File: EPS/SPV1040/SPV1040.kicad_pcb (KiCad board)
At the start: 2 copper layers, 17 parts, among them U1 SPV1040

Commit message: adding TSSOP8 footprint into SS footprint library for SPV1040. Also referenced footprint to the one in SS within the PCB layout
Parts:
- U1: footprint digikey-footprints:TSSOP-8_W4.4mm -> SS:TSSOP-8_W4.4mm

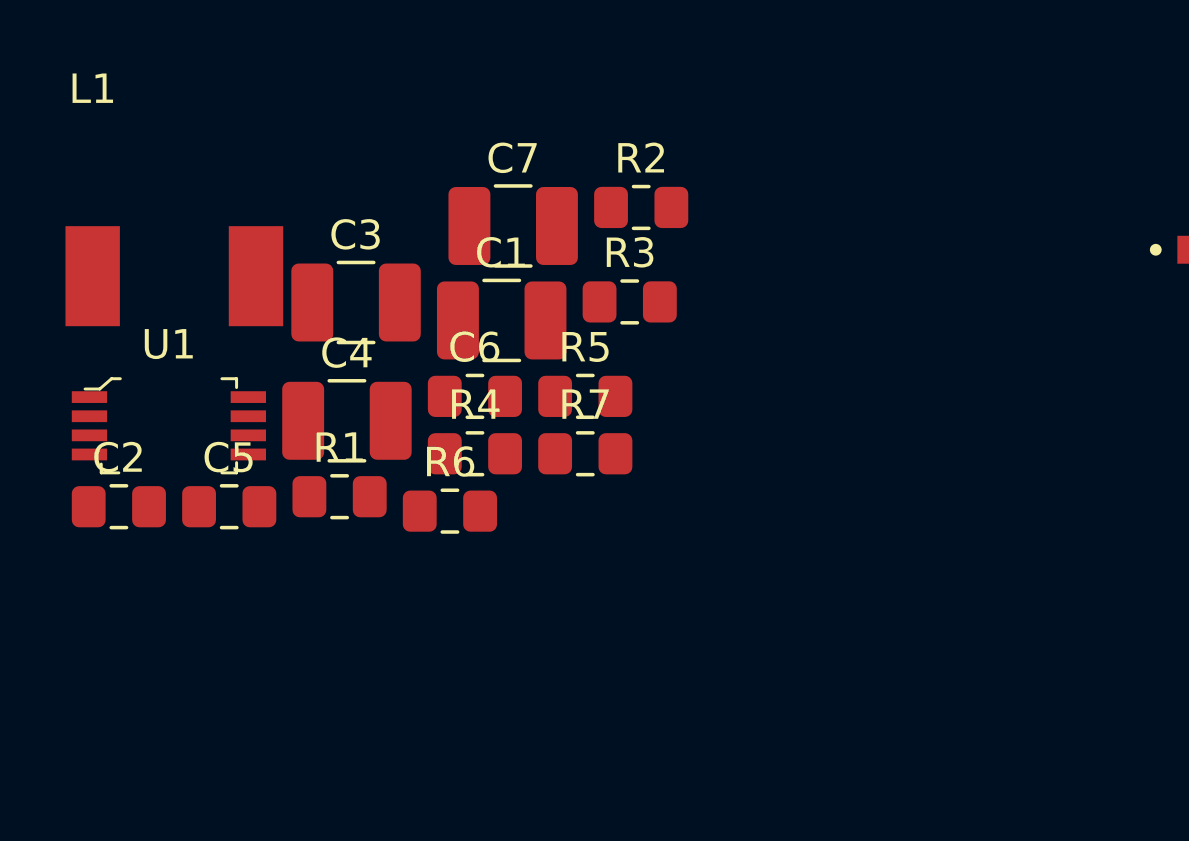
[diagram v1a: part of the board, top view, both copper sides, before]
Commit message: creating python script to find trace width for certian resistance. Also updating resistor divider feedback python to take user input to quit
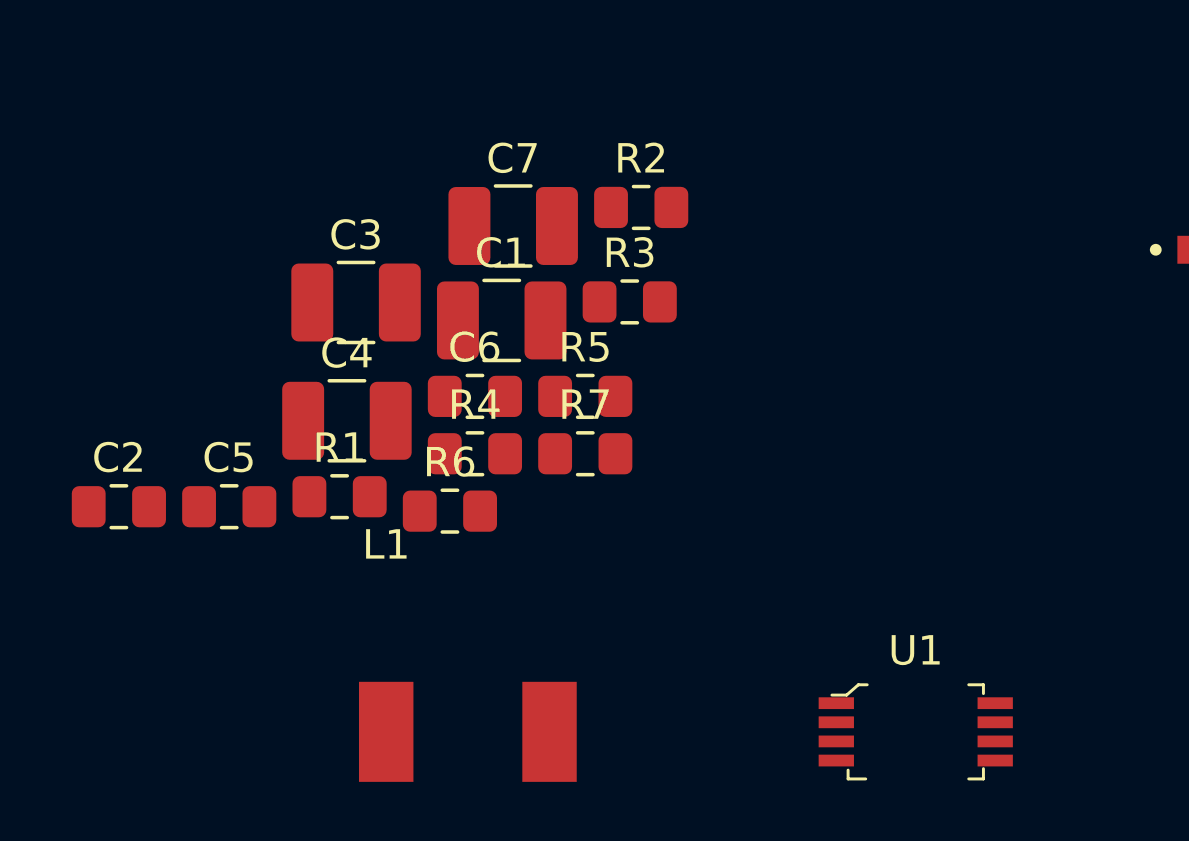
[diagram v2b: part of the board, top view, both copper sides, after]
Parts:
- moved U1 27.4 mm to (77.0, 57.9)
- moved L1 18.4 mm to (59.0, 57.9)
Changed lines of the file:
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@@
   )
   (module SS:TSSOP-8_W4.4mm (layer F.Cu)
-    (at 51.581001 47.511001)
+    (at 76.962 57.912)
     (descr http://www.st.com/content/ccc/resource/technical/document/datasheet/0d/30/c2/1a/92/03/48/cb/CD00287506.pdf/files/CD00287506.pdf/jcr:content/translations/en.CD00287506.pdf)
     (attr smd)
@@
   )
   (module SS:L_Bourns_6540 (layer F.Cu)
-    (at 48.991001 42.426001)
+    (at 58.966 57.912)
     (fp_text reference L1 (at 0 -6.35) (layer F.SilkS)
       (effects (font (size 1 1) (thickness 0.15)))

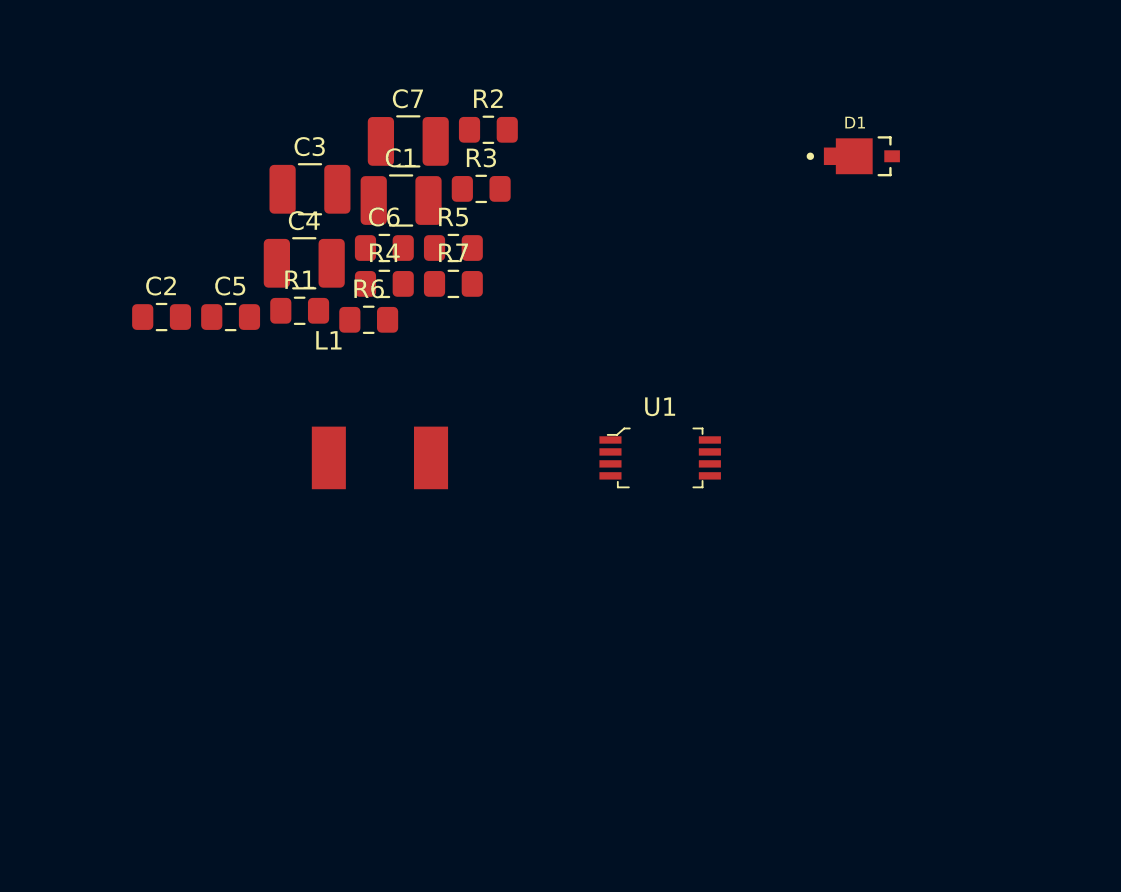
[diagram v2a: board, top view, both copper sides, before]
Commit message: completing PCB design for SPV1040, however this is designed for 0.6A output as appose to 0.7 since we do not have the right current sense resistor
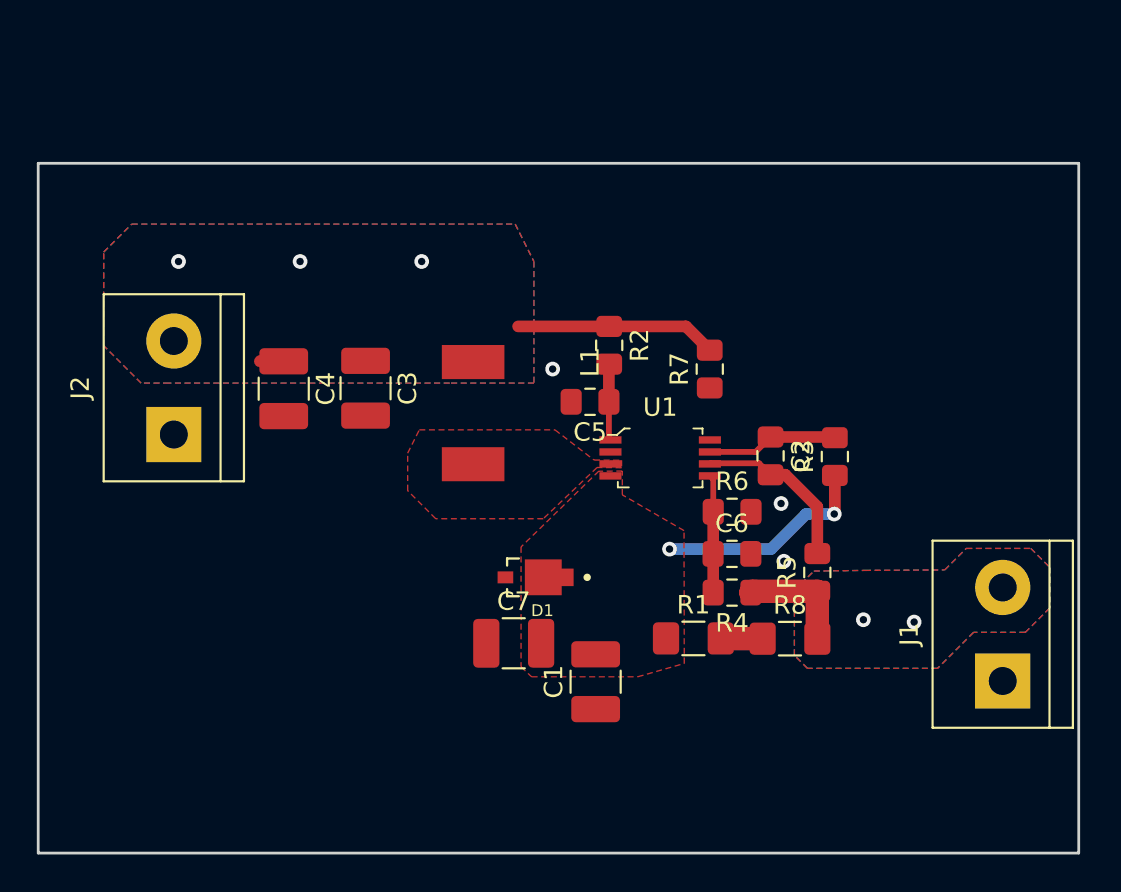
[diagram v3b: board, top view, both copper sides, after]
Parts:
- added J1: Screw_Terminal_01x02, TerminalBlock:TerminalBlock_bornier-2_P5.08mm, F.Cu at (95.6, 70.0)
- added J2: Screw_Terminal_01x02, TerminalBlock:TerminalBlock_bornier-2_P5.08mm, F.Cu at (50.5, 56.6)
- added R8: 0.039, Resistor_SMD:R_1206_3216Metric_Pad1.42x1.75mm_HandSolder, F.Cu at (84.0, 67.7)
- R1: value R_US -> 0.039; footprint Resistor_SMD:R_0805_2012Metric_Pad1.15x1.40mm_HandSolder -> Resistor_SMD:R_1206_3216Metric_Pad1.42x1.75mm_HandSolder
- moved C2 33.9 mm to (83.0, 57.8), turned to 270 degrees
- moved D1 28.9 mm to (70.2, 64.4), turned to 180 degrees
- moved C1 28.2 mm to (73.5, 70.1), turned to 90 degrees
- moved C7 27.9 mm to (69.0, 68.0)
- moved R1 27.8 mm to (78.8, 67.7)
- moved R5 26.5 mm to (85.5, 64.1), turned to 90 degrees
- moved R4 25.3 mm to (80.9, 65.2), turned to 180 degrees
- moved C6 25.1 mm to (80.9, 63.1)
- moved R3 24.1 mm to (86.4, 57.8), turned to 90 degrees
- moved R6 22.3 mm to (80.9, 60.8)
- moved C5 20.1 mm to (73.2, 54.9), turned to 180 degrees
- moved R7 14.7 mm to (79.7, 53.1), turned to 90 degrees
- moved R2 13.4 mm to (74.2, 51.8), turned to 270 degrees
- moved C3 11.2 mm to (61.0, 54.1), turned to 270 degrees
- moved L1 9.41 mm to (66.8, 52.7), turned to 270 degrees
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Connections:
- R1 pad 1: Net-(R1-Pad1) -> Net-(C1-Pad2)
- R1 pad 2: Net-(C1-Pad2) -> Net-(R1-Pad2)
- R4 pad 1: Net-(R1-Pad1) -> Net-(J1-Pad2)
- R5 pad 1: Net-(R1-Pad1) -> Net-(J1-Pad2)
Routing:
- net Net-(C1-Pad2): track 0.00 -> 12.6 mm, vias 0 -> 2
- net Net-(C3-Pad1): track 0.00 -> 11.0 mm, vias 0 -> 3
- net Net-(C2-Pad2): track 0.00 -> 9.37 mm
- net Net-(C2-Pad1): track 0.00 -> 7.14 mm
- net Net-(C6-Pad1): track 0.00 -> 6.69 mm
- net Net-(J1-Pad2): track 0.00 -> 6.24 mm, vias 0 -> 2
- net Net-(C5-Pad1): track 0.00 -> 4.16 mm
- net Net-(R1-Pad2): track 0.00 -> 2.27 mm
- net (no net): vias 0 -> 3
- added copper zone on F.Cu, net Net-(C1-Pad2)
- added copper zone on B.Cu, net Net-(C3-Pad1)
- added copper zone on F.Cu, net Net-(C3-Pad1)
- added copper zone on B.Cu, net Net-(J1-Pad2)
- added copper zone on F.Cu, net Net-(J1-Pad2)
- added copper zone on F.Cu, net Net-(L1-Pad2)
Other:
- board outline added: 56.5 x 37.5 mm
- net class Default: clearance 0.2 -> 0.2032
- rule trace_clearance: 0.2 -> 0.2032

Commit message: creating schematic for Lithion charger l6924 and adding schematic symbol into library ss
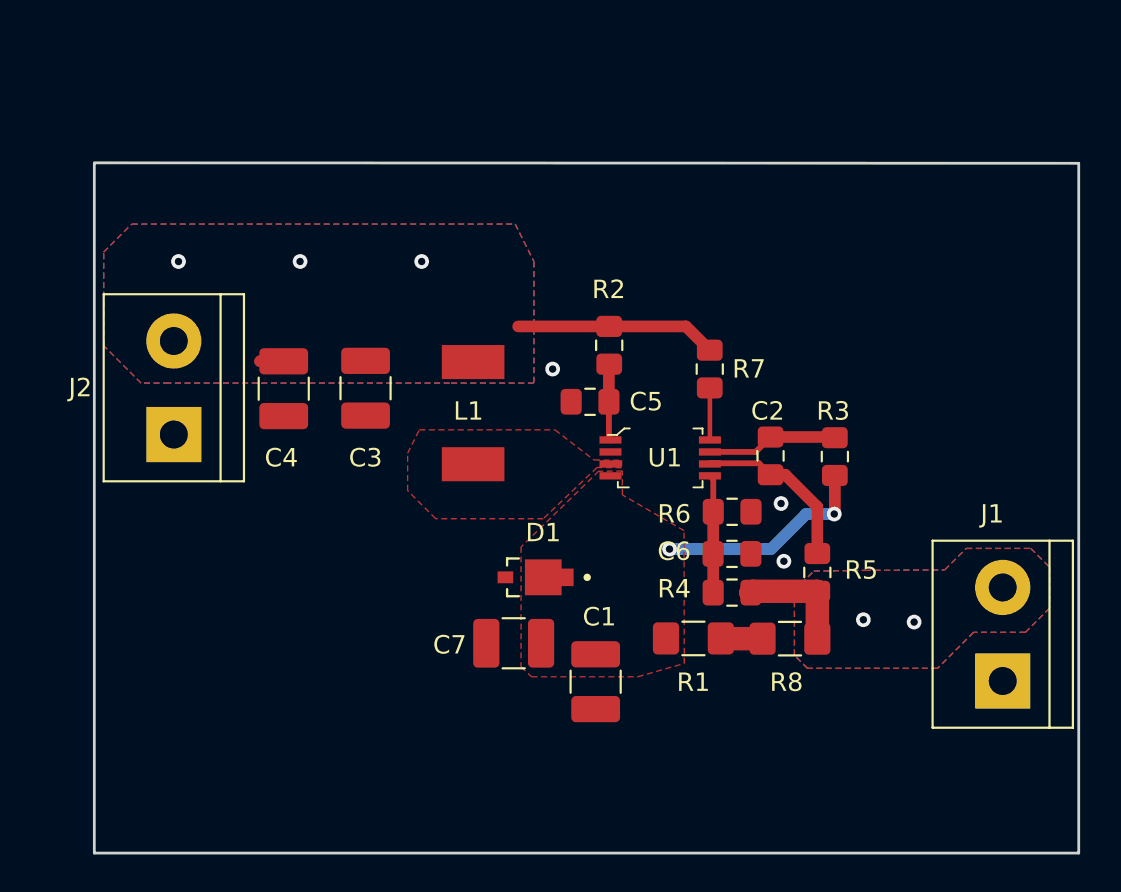
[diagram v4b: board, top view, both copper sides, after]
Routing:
- net Net-(R7-Pad1): track 0.01 -> 2.84 mm
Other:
- board size 56.5 x 37.5 mm -> 53.5 x 37.5 mm
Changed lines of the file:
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@@
     (thickness 1.6)
     (drawings 4)
-    (tracks 52)
+    (tracks 53)
     (zones 0)
     (modules 20)
@@
     (33 F.Adhes user hide)
     (34 B.Paste user hide)
-    (35 F.Paste user)
+    (35 F.Paste user hide)
     (36 B.SilkS user hide)
-    (37 F.SilkS user hide)
+    (37 F.SilkS user)
     (38 B.Mask user hide)
-    (39 F.Mask user)
+    (39 F.Mask user hide)
     (40 Dwgs.User user hide)
     (41 Cmts.User user hide)
@@
   )
   (setup
-    (last_trace_width 0.635)
+    (last_trace_width 0.25)
     (user_trace_width 0.1366)
     (user_trace_width 0.3175)
@@
     (tags "resistor handsolder")
     (attr smd)
-    (fp_text reference R8 (at 0 -1.82) (layer F.SilkS)
+    (fp_text reference R8 (at -0.1905 2.3749) (layer F.SilkS)
       (effects (font (size 1 1) (thickness 0.15)))
     )
@@
     (tags "resistor handsolder")
     (attr smd)
-    (fp_text reference R1 (at 0 -1.82) (layer F.SilkS)
+    (fp_text reference R1 (at 0 2.3876) (layer F.SilkS)
       (effects (font (size 1 1) (thickness 0.15)))
     )
@@
     (descr http://www.st.com/content/ccc/resource/technical/document/datasheet/0d/30/c2/1a/92/03/48/cb/CD00287506.pdf/files/CD00287506.pdf/jcr:content/translations/en.CD00287506.pdf)
     (attr smd)
-    (fp_text reference U1 (at 0 -2.75) (layer F.SilkS)
+    (fp_text reference U1 (at 0.254 0) (layer F.SilkS)
       (effects (font (size 1 1) (thickness 0.15)))
     )
@@
     (tags "capacitor handsolder")
     (attr smd)
-    (fp_text reference C1 (at 0 -2.28 90) (layer F.SilkS)
+    (fp_text reference C1 (at 3.5195 0.2032 180) (layer F.SilkS)
       (effects (font (size 1 1) (thickness 0.15)))
     )
@@
     (tags "capacitor handsolder")
     (attr smd)
-    (fp_text reference C2 (at 0 -1.65 270) (layer F.SilkS)
+    (fp_text reference C2 (at -2.4294 0.1524) (layer F.SilkS)
       (effects (font (size 1 1) (thickness 0.15)))
     )
@@
     (tags "capacitor handsolder")
     (attr smd)
-    (fp_text reference C3 (at 0 -2.28 270) (layer F.SilkS)
+    (fp_text reference C3 (at 3.7846 0) (layer F.SilkS)
       (effects (font (size 1 1) (thickness 0.15)))
     )
@@
     (tags "capacitor handsolder")
     (attr smd)
-    (fp_text reference C4 (at 0 -2.28 270) (layer F.SilkS)
+    (fp_text reference C4 (at 3.7592 0.127) (layer F.SilkS)
       (effects (font (size 1 1) (thickness 0.15)))
     )
@@
     (tags "capacitor handsolder")
     (attr smd)
-    (fp_text reference C5 (at 0 -1.65 180) (layer F.SilkS)
+    (fp_text reference C5 (at -3.048 0 180) (layer F.SilkS)
       (effects (font (size 1 1) (thickness 0.15)))
     )
@@
     (tags "capacitor handsolder")
     (attr smd)
-    (fp_text reference C6 (at 0 -1.65) (layer F.SilkS)
+    (fp_text reference C6 (at -3.136307 -0.132393) (layer F.SilkS)
       (effects (font (size 1 1) (thickness 0.15)))
     )
@@
     (tags "capacitor handsolder")
     (attr smd)
-    (fp_text reference C7 (at 0 -2.28) (layer F.SilkS)
+    (fp_text reference C7 (at -3.474338 0.092055) (layer F.SilkS)
       (effects (font (size 1 1) (thickness 0.15)))
     )
@@
   (module SS:DIO_SMM4F5.0A-TR (layer F.Cu)
     (at 70.197 64.398545 180)
-    (fp_text reference D1 (at -0.368 -1.8064 180) (layer F.SilkS)
-      (effects (font (size 0.64 0.64) (thickness 0.015)))
+    (fp_text reference D1 (at -0.415 2.422545 180) (layer F.SilkS)
+      (effects (font (size 1 1) (thickness 0.15)))
     )
     (fp_text value SMM4F5.0 (at 4.1024 1.6936 180) (layer F.Fab)
@@
   (module SS:L_Bourns_6540 (layer F.Cu)
     (at 66.802 52.705 270)
-    (fp_text reference L1 (at 0 -6.35 270) (layer F.SilkS)
+    (fp_text reference L1 (at 2.667 0.254) (layer F.SilkS)
       (effects (font (size 1 1) (thickness 0.15)))
     )
@@
     (tags "resistor handsolder")
     (attr smd)
-    (fp_text reference R2 (at 0 -1.65 270) (layer F.SilkS)
+    (fp_text reference R2 (at -3.0263 0.0254) (layer F.SilkS)
       (effects (font (size 1 1) (thickness 0.15)))
     )
@@
     (tags "resistor handsolder")
     (attr smd)
-    (fp_text reference R3 (at 0 -1.65 90) (layer F.SilkS)
+    (fp_text reference R3 (at 2.4675 -0.0889 180) (layer F.SilkS)
       (effects (font (size 1 1) (thickness 0.15)))
     )
@@
     (tags "resistor handsolder")
     (attr smd)
-    (fp_text reference R4 (at 0 -1.65 180) (layer F.SilkS)
+    (fp_text reference R4 (at 3.1406 0.2032 180) (layer F.SilkS)
       (effects (font (size 1 1) (thickness 0.15)))
     )
@@
     (tags "resistor handsolder")
     (attr smd)
-    (fp_text reference R5 (at 0 -1.65 90) (layer F.SilkS)
+    (fp_text reference R5 (at 0.1233 2.3876 180) (layer F.SilkS)
       (effects (font (size 1 1) (thickness 0.15)))
     )
@@
     (tags "resistor handsolder")
     (attr smd)
-    (fp_text reference R6 (at 0 -1.65) (layer F.SilkS)
+    (fp_text reference R6 (at -3.145307 0.121607) (layer F.SilkS)
       (effects (font (size 1 1) (thickness 0.15)))
     )
@@
     (tags "resistor handsolder")
     (attr smd)
-    (fp_text reference R7 (at 0 -1.65 90) (layer F.SilkS)
+    (fp_text reference R7 (at 0 2.1336 180) (layer F.SilkS)
       (effects (font (size 1 1) (thickness 0.15)))
     )
@@
     (descr "simple 2-pin terminal block, pitch 5.08mm, revamped version of bornier2")
     (tags "terminal block bornier2")
-    (fp_text reference J1 (at 2.54 -5.08 90) (layer F.SilkS)
+    (fp_text reference J1 (at 9.0678 -0.5715 180) (layer F.SilkS)
       (effects (font (size 1 1) (thickness 0.15)))
     )
@@
     (descr "simple 2-pin terminal block, pitch 5.08mm, revamped version of bornier2")
     (tags "terminal block bornier2")
-    (fp_text reference J2 (at 2.54 -5.08 90) (layer F.SilkS)
+    (fp_text reference J2 (at 2.54 -5.08 180) (layer F.SilkS)
       (effects (font (size 1 1) (thickness 0.15)))
     )
@@
     )
   )
-  (gr_line (start 43.18 79.375) (end 43.18 41.91) (layer Edge.Cuts) (width 0.15))
-  (gr_line (start 99.695 79.375) (end 43.18 79.375) (layer Edge.Cuts) (width 0.15))
+  (gr_line (start 46.228 79.375) (end 46.228 41.91) (layer Edge.Cuts) (width 0.15))
+  (gr_line (start 99.695 79.375) (end 46.228 79.375) (layer Edge.Cuts) (width 0.15))
   (gr_line (start 99.695 41.91) (end 99.695 79.375) (layer Edge.Cuts) (width 0.15))
-  (gr_line (start 43.18 41.91) (end 99.695 41.91) (layer Edge.Cuts) (width 0.15))
+  (gr_line (start 46.228 41.8846) (end 99.695 41.91) (layer Edge.Cuts) (width 0.15))
   (via (at 83.5279 60.3885) (size 0.8) (drill 0.4) (layers F.Cu B.Cu) (net 0))
   (via (at 83.6803 63.5254) (size 0.8) (drill 0.4) (layers F.Cu B.Cu) (net 0))
@@
   (segment (start 79.8396 60.8431) (end 79.844307 60.838393) (width 0.635) (layer F.Cu) (net 7))
   (segment (start 79.8396 65.2272) (end 79.8396 60.8431) (width 0.635) (layer F.Cu) (net 7))
-  (segment (start 68.0668 58.237) (end 68.0466 58.2168) (width 0.25) (layer F.Cu) (net 8))
   (segment (start 79.6544 56.9294) (end 79.662 56.937) (width 0.3175) (layer F.Cu) (net 9))
+  (segment (start 79.662 54.1186) (end 79.6544 54.111) (width 0.25) (layer F.Cu) (net 9))
+  (segment (start 79.662 56.937) (end 79.662 54.1186) (width 0.25) (layer F.Cu) (net 9))
   (segment (start 80.2672 67.7291) (end 80.2545 67.7164) (width 1.27) (layer F.Cu) (net 10))
   (segment (start 82.523 67.7291) (end 80.2672 67.7291) (width 1.27) (layer F.Cu) (net 10))
